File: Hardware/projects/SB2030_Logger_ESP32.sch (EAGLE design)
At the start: 105 parts, among them T2 S8050, T3 S8050, T4 S8050, U1 ESP32-WROOM-32E, U2 TJA1051T/3, U3 LSM6DS3TR-C, U4 AMS1117-3.3, U5 SN65C1168NSR

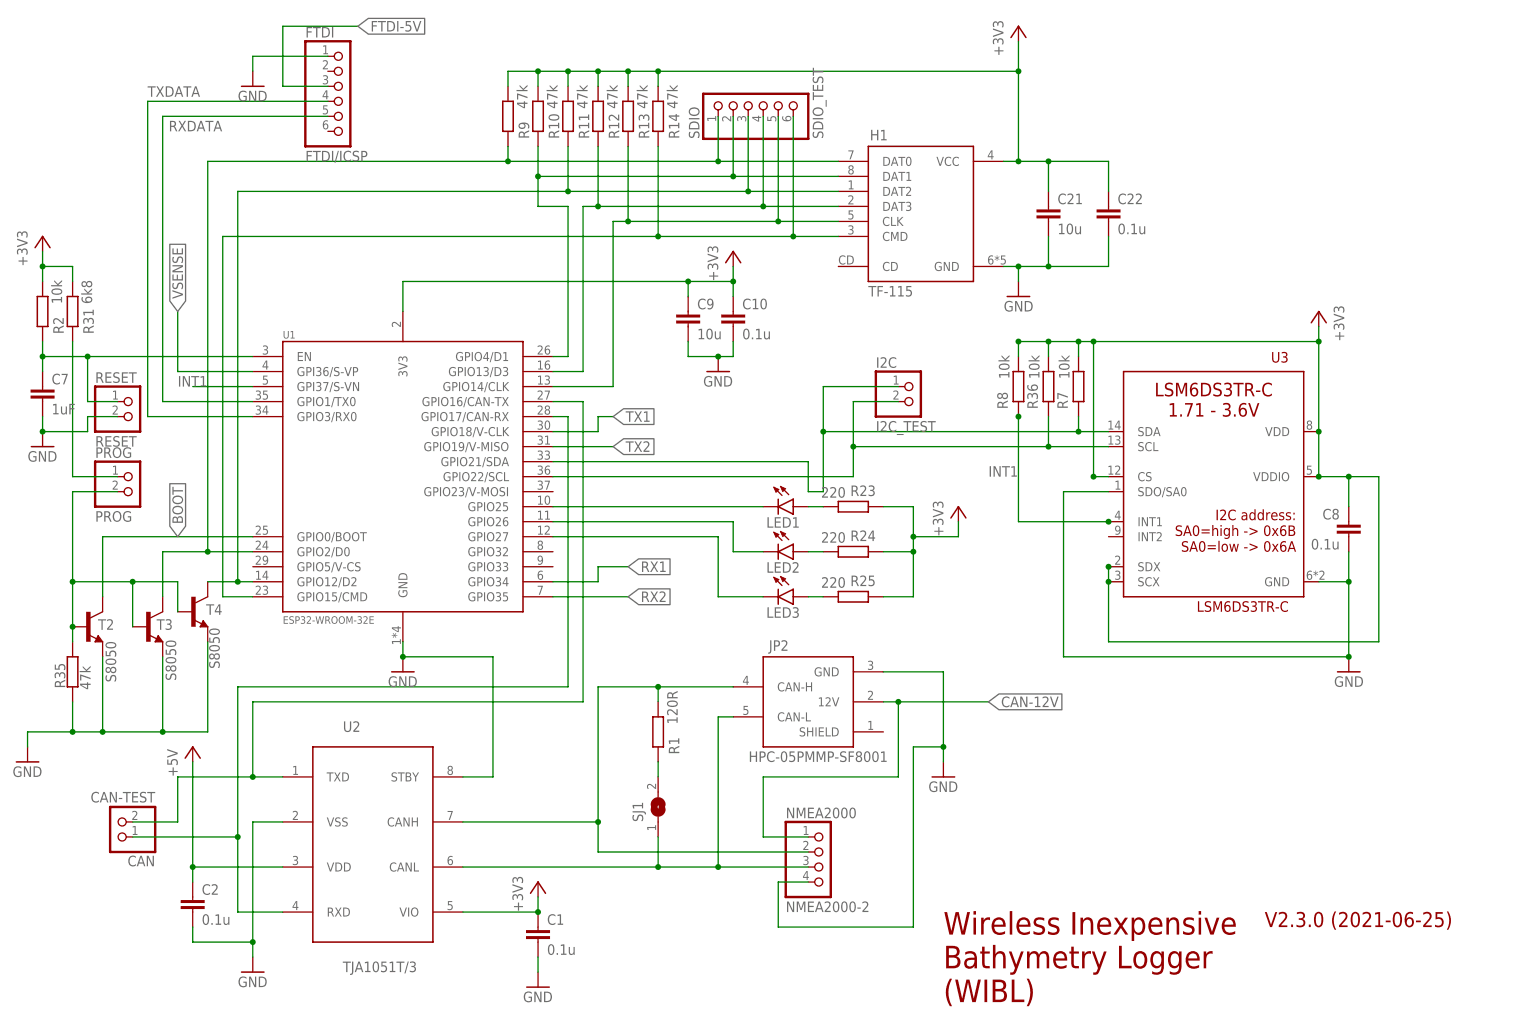
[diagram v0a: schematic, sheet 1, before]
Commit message: Fixed labelling on schematic for INT1 from IMU, and cleaned up some notation; fixed routing and airwires on board so that DRC passes.
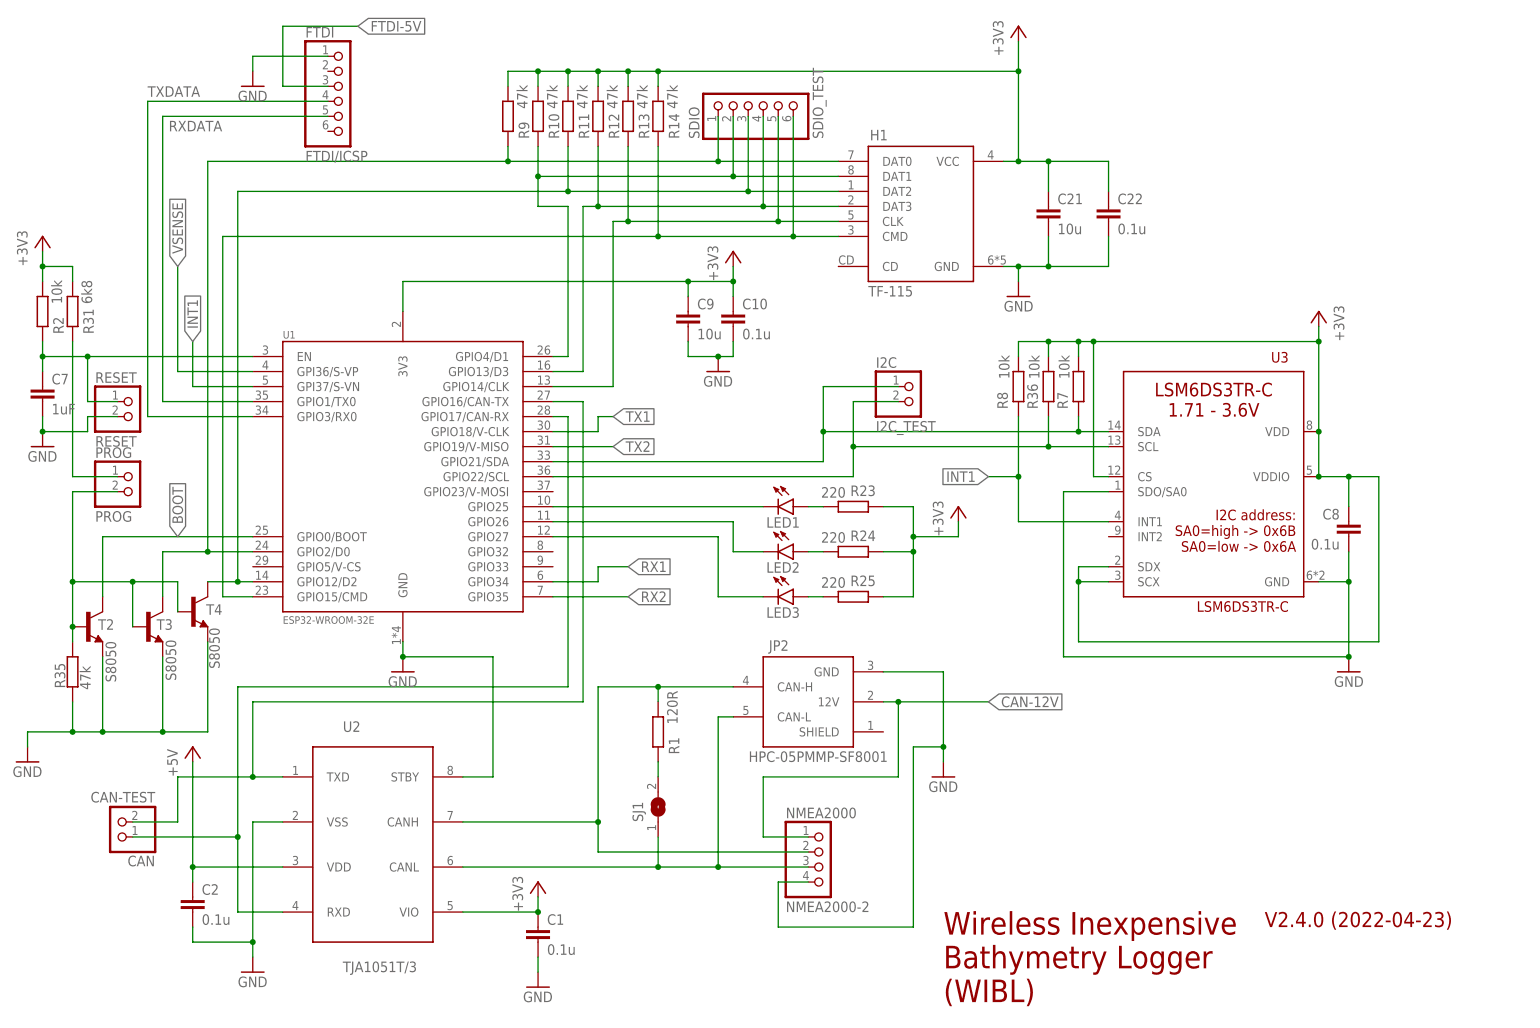
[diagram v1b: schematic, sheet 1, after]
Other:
- note added: "V 2.4.0 (2022-04-23)"
- note added: "V2.4.0 (2022-04-23)"
- note removed: "V 2.3.0 (2021-06-25)"
- note removed: "V2.3.0 (2021-06-25)"
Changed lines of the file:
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@@
 Bathymetry Logger
 (WIBL)</text>
-<text x="216.916" y="20.32" size="2.54" layer="94">V2.3.0 (2021-06-25)</text>
+<text x="216.916" y="20.32" size="2.54" layer="94">V2.4.0 (2022-04-23)</text>
 </plain>
 <instances>
@@
 <wire x1="226.06" y1="119.38" x2="226.06" y2="121.92" width="0.1524" layer="91"/>
 <wire x1="226.06" y1="96.52" x2="226.06" y2="104.14" width="0.1524" layer="91"/>
-<pinref part="U3" gate="G$1" pin="SDX"/>
-<pinref part="U3" gate="G$1" pin="SCX"/>
-<wire x1="190.5" y1="81.28" x2="190.5" y2="78.74" width="0.1524" layer="91"/>
-<wire x1="190.5" y1="78.74" x2="190.5" y2="68.58" width="0.1524" layer="91"/>
-<wire x1="190.5" y1="68.58" x2="236.22" y2="68.58" width="0.1524" layer="91"/>
-<junction x="190.5" y="78.74"/>
+<wire x1="185.42" y1="68.58" x2="236.22" y2="68.58" width="0.1524" layer="91"/>
 <wire x1="236.22" y1="68.58" x2="236.22" y2="96.52" width="0.1524" layer="91"/>
 <wire x1="236.22" y1="96.52" x2="231.14" y2="96.52" width="0.1524" layer="91"/>
@@
 <wire x1="231.14" y1="91.44" x2="231.14" y2="96.52" width="0.1524" layer="91"/>
 <junction x="231.14" y="96.52"/>
-<junction x="190.5" y="81.28"/>
 <wire x1="226.06" y1="119.38" x2="187.96" y2="119.38" width="0.1524" layer="91"/>
 <junction x="226.06" y="119.38"/>
-<pinref part="R8" gate="G$1" pin="2"/>
 <wire x1="187.96" y1="119.38" x2="185.42" y2="119.38" width="0.1524" layer="91"/>
 <wire x1="185.42" y1="119.38" x2="180.34" y2="119.38" width="0.1524" layer="91"/>
-<wire x1="180.34" y1="119.38" x2="175.26" y2="119.38" width="0.1524" layer="91"/>
-<wire x1="175.26" y1="119.38" x2="175.26" y2="116.84" width="0.1524" layer="91"/>
 <pinref part="R36" gate="G$1" pin="2"/>
 <wire x1="180.34" y1="116.84" x2="180.34" y2="119.38" width="0.1524" layer="91"/>
-<junction x="180.34" y="119.38"/>
 <pinref part="R7" gate="G$1" pin="2"/>
 <wire x1="185.42" y1="116.84" x2="185.42" y2="119.38" width="0.1524" layer="91"/>
 <junction x="185.42" y="119.38"/>
-<junction x="175.26" y="119.38"/>
 <pinref part="U3" gate="G$1" pin="CS"/>
 <wire x1="190.5" y1="96.52" x2="187.96" y2="96.52" width="0.1524" layer="91"/>
 <wire x1="187.96" y1="96.52" x2="187.96" y2="119.38" width="0.1524" layer="91"/>
 <junction x="187.96" y="119.38"/>
-<junction x="187.96" y="96.52"/>
+<pinref part="R8" gate="G$1" pin="2"/>
+<wire x1="175.26" y1="119.38" x2="175.26" y2="116.84" width="0.1524" layer="91"/>
+<wire x1="180.34" y1="119.38" x2="175.26" y2="119.38" width="0.1524" layer="91"/>
+<junction x="180.34" y="119.38"/>
+<pinref part="U3" gate="G$1" pin="SDX"/>
+<wire x1="190.5" y1="81.28" x2="185.42" y2="81.28" width="0.1524" layer="91"/>
+<wire x1="185.42" y1="81.28" x2="185.42" y2="78.74" width="0.1524" layer="91"/>
+<wire x1="185.42" y1="78.74" x2="185.42" y2="68.58" width="0.1524" layer="91"/>
+<pinref part="U3" gate="G$1" pin="SCX"/>
+<wire x1="190.5" y1="78.74" x2="185.42" y2="78.74" width="0.1524" layer="91"/>
+<junction x="185.42" y="78.74"/>
 </segment>
 <segment>
@@
 <net name="VSENSE" class="0">
 <segment>
-<wire x1="33.02" y1="114.3" x2="33.02" y2="124.46" width="0.1524" layer="91"/>
-<label x="33.02" y="124.46" size="1.778" layer="95" rot="R90" xref="yes"/>
+<wire x1="33.02" y1="114.3" x2="33.02" y2="132.08" width="0.1524" layer="91"/>
+<label x="33.02" y="132.08" size="1.778" layer="95" rot="R90" xref="yes"/>
 <wire x1="45.72" y1="114.3" x2="33.02" y2="114.3" width="0.1524" layer="91"/>
 <pinref part="U1" gate="G$1" pin="GPI36/S-VP"/>
@@
 <wire x1="154.94" y1="111.76" x2="142.24" y2="111.76" width="0.1524" layer="91"/>
 <wire x1="142.24" y1="111.76" x2="142.24" y2="104.14" width="0.1524" layer="91"/>
-<wire x1="142.24" y1="104.14" x2="142.24" y2="93.98" width="0.1524" layer="91"/>
-<wire x1="96.52" y1="99.06" x2="139.7" y2="99.06" width="0.1524" layer="91"/>
-<wire x1="139.7" y1="99.06" x2="139.7" y2="93.98" width="0.1524" layer="91"/>
-<wire x1="139.7" y1="93.98" x2="142.24" y2="93.98" width="0.1524" layer="91"/>
+<wire x1="142.24" y1="104.14" x2="142.24" y2="99.06" width="0.1524" layer="91"/>
+<wire x1="96.52" y1="99.06" x2="142.24" y2="99.06" width="0.1524" layer="91"/>
 <pinref part="U1" gate="G$1" pin="GPIO21/SDA"/>
 <pinref part="R7" gate="G$1" pin="1"/>
@@
 <segment>
 <pinref part="U3" gate="G$1" pin="INT1"/>
+<wire x1="190.5" y1="88.9" x2="175.26" y2="88.9" width="0.1524" layer="91"/>
 <pinref part="R8" gate="G$1" pin="1"/>
-<wire x1="190.5" y1="88.9" x2="175.26" y2="88.9" width="0.1524" layer="91"/>
-<wire x1="175.26" y1="88.9" x2="175.26" y2="106.68" width="0.1524" layer="91"/>
-<junction x="175.26" y="106.68"/>
-<junction x="190.5" y="88.9"/>
-<label x="170.18" y="96.52" size="1.778" layer="95"/>
+<wire x1="175.26" y1="106.68" x2="175.26" y2="96.52" width="0.1524" layer="91"/>
+<wire x1="175.26" y1="96.52" x2="175.26" y2="88.9" width="0.1524" layer="91"/>
+<wire x1="175.26" y1="96.52" x2="170.18" y2="96.52" width="0.1524" layer="91"/>
+<junction x="175.26" y="96.52"/>
+<label x="170.18" y="96.52" size="1.778" layer="95" rot="R180" xref="yes"/>
 </segment>
 <segment>
 <pinref part="U1" gate="G$1" pin="GPI37/S-VN"/>
 <wire x1="45.72" y1="111.76" x2="35.56" y2="111.76" width="0.1524" layer="91"/>
-<label x="33.02" y="111.76" size="1.778" layer="95"/>
+<wire x1="35.56" y1="111.76" x2="35.56" y2="119.38" width="0.1524" layer="91"/>
+<label x="35.56" y="119.38" size="1.778" layer="95" rot="R90" xref="yes"/>
 </segment>
 </net>
@@
 Bathymetry Logger
 (WIBL)</text>
-<text x="168.656" y="-10.16" size="2.54" layer="94">V 2.3.0 (2021-06-25)</text>
+<text x="168.656" y="-10.16" size="2.54" layer="94">V 2.4.0 (2022-04-23)</text>
 </plain>
 <instances>
